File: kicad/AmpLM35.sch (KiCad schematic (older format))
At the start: 15 parts, among them P2 CONN_01X03, U1 OP07, U2 OP07

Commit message: circuito y pcb terminado.
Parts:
- removed P2: CONN_01X03, Pin_Headers:Pin_Header_Straight_1x03, symbol CONN_01X03
- added U6: LM35, TO_SOT_Packages_THT:TO-92_Inline_Wide, symbol LM35
- added W1: Lm1, Measurement_Points:Measurement_Point_Round-SMD-Pad_Big, symbol TEST_1P
- added W2: Lm2, Measurement_Points:Measurement_Point_Round-SMD-Pad_Big, symbol TEST_1P
- added W3: Lm3, Measurement_Points:Measurement_Point_Round-SMD-Pad_Big, symbol TEST_1P
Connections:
- net +5V: now also U6.1 (+Vs)
- net GNDA: now also U6.3 (GND)
- net LM35_OUT: now also W3.1
- net at U1.3 (+): now also U6.2 (Vout), W1.1
- net at R2.1, R3.2, U1.6: now also W2.1
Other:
- note added: "Capacitores de desacople\nDeben estar junto a U1"
- note added: "Capacitores de desacople\nDeben estar junto a U2"
- note added: "LM35 junto a la \nbornera de la \ntermocupla"
- note removed: "Capacitores de desacople\nEn el PCB deben estar junto a U1"
- note removed: "Capacitores de desacople\nEn el PCB deben estar junto a U2"
- note removed: "Conexión del LM35"
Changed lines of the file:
@@
 $Descr A4 11693 8268
 encoding utf-8
-Sheet 3 5
+Sheet 2 5
 Title "Amplificador y filtro del sensor LM35"
-Date "2016-08-27"
-Rev "1"
+Date "2016-09-11"
+Rev "2"
 Comp "Elián Hanisch - Rodrigo Oliver - Gastón Riera"
 Comment1 "Cátedra de Proyecto Final"
@@
 	1    0    0    -1
 $EndComp
-Text HLabel 2750 1850 0    60   Input ~ 0
-+5V
-Text HLabel 2750 2000 0    60   Input ~ 0
--5V
-Text HLabel 2750 2150 0    60   Input ~ 0
-GND
-$Comp
-L -5V #PWR6
-U 1 1 57C21C1D
-P 3350 1600
-F 0 "#PWR6" H 3350 1700 50  0001 C CNN
-F 1 "-5V" H 3350 1750 50  0000 C CNN
-F 2 "" H 3350 1600 50  0000 C CNN
-F 3 "" H 3350 1600 50  0000 C CNN
-	1    3350 1600
-	1    0    0    -1
-$EndComp
-$Comp
-L +5V #PWR03
-U 1 1 57C21BA8
-P 3100 1600
-F 0 "#PWR03" H 3100 1450 50  0001 C CNN
-F 1 "+5V" H 3100 1740 50  0000 C CNN
-F 2 "" H 3100 1600 50  0000 C CNN
-F 3 "" H 3100 1600 50  0000 C CNN
-	1    3100 1600
-	1    0    0    -1
-$EndComp
-$Comp
-L +5V #PWR04
+$Comp
+L +5V #PWR07
 U 1 1 57C21C9E
-P 1800 3100
-F 0 "#PWR04" H 1800 2950 50  0001 C CNN
-F 1 "+5V" H 1800 3240 50  0000 C CNN
-F 2 "" H 1800 3100 50  0000 C CNN
-F 3 "" H 1800 3100 50  0000 C CNN
-	1    1800 3100
-	1    0    0    -1
-$EndComp
-$Comp
-L -5V #PWR20
+P 2500 2950
+F 0 "#PWR07" H 2500 2800 50  0001 C CNN
+F 1 "+5V" H 2500 3090 50  0000 C CNN
+F 2 "" H 2500 2950 50  0000 C CNN
+F 3 "" H 2500 2950 50  0000 C CNN
+	1    2500 2950
+	1    0    0    -1
+$EndComp
+$Comp
+L -5V #PWR22
 U 1 1 57C21D19
 P 7850 3850
-F 0 "#PWR20" H 7850 3950 50  0001 C CNN
+F 0 "#PWR22" H 7850 3950 50  0001 C CNN
 F 1 "-5V" H 7850 4000 50  0000 C CNN
 F 2 "" H 7850 3850 50  0000 C CNN
@@
 $EndComp
 $Comp
-L -5V #PWR10
+L -5V #PWR12
 U 1 1 57C21D33
 P 4750 3800
-F 0 "#PWR10" H 4750 3900 50  0001 C CNN
+F 0 "#PWR12" H 4750 3900 50  0001 C CNN
 F 1 "-5V" H 4750 3950 50  0000 C CNN
 F 2 "" H 4750 3800 50  0000 C CNN
@@
 $EndComp
 $Comp
-L +5V #PWR05
+L +5V #PWR08
 U 1 1 57C21D4D
 P 4750 3150
-F 0 "#PWR05" H 4750 3000 50  0001 C CNN
+F 0 "#PWR08" H 4750 3000 50  0001 C CNN
 F 1 "+5V" H 4750 3290 50  0000 C CNN
 F 2 "" H 4750 3150 50  0000 C CNN
@@
 $EndComp
 $Comp
-L +5V #PWR06
+L +5V #PWR09
 U 1 1 57C21D67
 P 7850 3250
-F 0 "#PWR06" H 7850 3100 50  0001 C CNN
+F 0 "#PWR09" H 7850 3100 50  0001 C CNN
 F 1 "+5V" H 7850 3390 50  0000 C CNN
 F 2 "" H 7850 3250 50  0000 C CNN
@@
 LM35_OUT
 $Comp
-L GNDA #PWR07
+L GNDA #PWR010
 U 1 1 57C21F0E
-P 1800 3600
-F 0 "#PWR07" H 1800 3350 50  0001 C CNN
-F 1 "GNDA" H 1800 3450 50  0000 C CNN
-F 2 "" H 1800 3600 50  0000 C CNN
-F 3 "" H 1800 3600 50  0000 C CNN
-	1    1800 3600
-	1    0    0    -1
-$EndComp
-$Comp
-L GNDA #PWR08
-U 1 1 57C21F2C
-P 3350 2250
-F 0 "#PWR08" H 3350 2000 50  0001 C CNN
-F 1 "GNDA" H 3350 2100 50  0000 C CNN
-F 2 "" H 3350 2250 50  0000 C CNN
-F 3 "" H 3350 2250 50  0000 C CNN
-	1    3350 2250
+P 2500 3750
+F 0 "#PWR010" H 2500 3500 50  0001 C CNN
+F 1 "GNDA" H 2500 3600 50  0000 C CNN
+F 2 "" H 2500 3750 50  0000 C CNN
+F 3 "" H 2500 3750 50  0000 C CNN
+	1    2500 3750
 	1    0    0    -1
 $EndComp
@@
 $EndComp
 $Comp
-L GNDA #PWR09
+L GNDA #PWR011
 U 1 1 57C224B9
 P 7300 4550
-F 0 "#PWR09" H 7300 4300 50  0001 C CNN
+F 0 "#PWR011" H 7300 4300 50  0001 C CNN
 F 1 "GNDA" H 7300 4400 50  0000 C CNN
 F 2 "" H 7300 4550 50  0000 C CNN
@@
 $EndComp
 $Comp
-L GNDA #PWR010
+L GNDA #PWR012
 U 1 1 57C228B2
 P 3900 4800
-F 0 "#PWR010" H 3900 4550 50  0001 C CNN
+F 0 "#PWR012" H 3900 4550 50  0001 C CNN
 F 1 "GNDA" H 3900 4650 50  0000 C CNN
 F 2 "" H 3900 4800 50  0000 C CNN
@@
 P 8200 4750
 F 0 "RV2" H 8200 4670 50  0000 C CNN
-F 1 "POT" H 8200 4750 50  0000 C CNN
+F 1 "POT" H 8200 4750 50  0001 C CNN
 F 2 "Potentiometers:Potentiometer_Bourns_3005_Angular_ScrewFront" H 8200 4750 50  0001 C CNN
 F 3 "" H 8200 4750 50  0000 C CNN
@@
 $EndComp
 $Comp
-L +5V #PWR011
+L +5V #PWR013
 U 1 1 57C51F8E
 P 8350 4450
-F 0 "#PWR011" H 8350 4300 50  0001 C CNN
+F 0 "#PWR013" H 8350 4300 50  0001 C CNN
 F 1 "+5V" H 8350 4590 50  0000 C CNN
 F 2 "" H 8350 4450 50  0000 C CNN
@@
 P 5100 4750
 F 0 "RV1" H 5100 4670 50  0000 C CNN
-F 1 "POT" H 5100 4750 50  0000 C CNN
+F 1 "POT" H 5100 4750 50  0001 C CNN
 F 2 "Potentiometers:Potentiometer_Bourns_3005_Angular_ScrewFront" H 5100 4750 50  0001 C CNN
 F 3 "" H 5100 4750 50  0000 C CNN
@@
 $EndComp
 $Comp
-L +5V #PWR012
+L +5V #PWR014
 U 1 1 57C5230B
 P 5250 4450
-F 0 "#PWR012" H 5250 4300 50  0001 C CNN
+F 0 "#PWR014" H 5250 4300 50  0001 C CNN
 F 1 "+5V" H 5250 4590 50  0000 C CNN
 F 2 "" H 5250 4450 50  0000 C CNN
@@
 	1    0    0    -1
 $EndComp
-$Comp
-L CONN_01X03 P2
-U 1 1 57C53794
-P 1550 3350
-F 0 "P2" H 1550 3550 50  0000 C CNN
-F 1 "CONN_01X03" V 1650 3350 50  0000 C CNN
-F 2 "Pin_Headers:Pin_Header_Straight_1x03" H 1550 3350 50  0001 C CNN
-F 3 "" H 1550 3350 50  0000 C CNN
-	1    1550 3350
-	-1   0    0    1
-$EndComp
-Text Notes 1500 2850 0    60   ~ 0
-Conexión del LM35
+Text Notes 2250 4250 0    60   ~ 0
+LM35 junto a la \nbornera de la \ntermocupla
 Text Notes 7500 2600 0    60   ~ 0
 Filtro pasa-bajos\nFc = 2Hz\nAtt@50hz = 40dB
@@
 $EndComp
 $Comp
-L GNDA #PWR013
+L GNDA #PWR015
 U 1 1 57C5CD5D
 P 7800 5750
-F 0 "#PWR013" H 7800 5500 50  0001 C CNN
+F 0 "#PWR015" H 7800 5500 50  0001 C CNN
 F 1 "GNDA" H 7800 5600 50  0000 C CNN
 F 2 "" H 7800 5750 50  0000 C CNN
@@
 $EndComp
 $Comp
-L GNDA #PWR014
+L GNDA #PWR016
 U 1 1 57C5CD63
 P 8200 5750
-F 0 "#PWR014" H 8200 5500 50  0001 C CNN
+F 0 "#PWR016" H 8200 5500 50  0001 C CNN
 F 1 "GNDA" H 8200 5600 50  0000 C CNN
 F 2 "" H 8200 5750 50  0000 C CNN
@@
 $EndComp
 $Comp
-L +5V #PWR015
+L +5V #PWR017
 U 1 1 57C5CD69
 P 7800 5450
-F 0 "#PWR015" H 7800 5300 50  0001 C CNN
+F 0 "#PWR017" H 7800 5300 50  0001 C CNN
 F 1 "+5V" H 7800 5590 50  0000 C CNN
 F 2 "" H 7800 5450 50  0000 C CNN
@@
 $EndComp
 $Comp
-L -5V #PWR21
+L -5V #PWR23
 U 1 1 57C5CD6F
 P 8200 5450
-F 0 "#PWR21" H 8200 5550 50  0001 C CNN
+F 0 "#PWR23" H 8200 5550 50  0001 C CNN
 F 1 "-5V" H 8200 5600 50  0000 C CNN
 F 2 "" H 8200 5450 50  0000 C CNN
@@
 $EndComp
 Text Notes 7750 6150 0    60   ~ 0
-Capacitores de desacople\nEn el PCB deben estar junto a U2
+Capacitores de desacople\nDeben estar junto a U2
 $Comp
 L C C5
@@
 $EndComp
 $Comp
-L GNDA #PWR016
+L GNDA #PWR018
 U 1 1 57C5D25F
 P 4900 5750
-F 0 "#PWR016" H 4900 5500 50  0001 C CNN
+F 0 "#PWR018" H 4900 5500 50  0001 C CNN
 F 1 "GNDA" H 4900 5600 50  0000 C CNN
 F 2 "" H 4900 5750 50  0000 C CNN
@@
 $EndComp
 $Comp
-L GNDA #PWR017
+L GNDA #PWR019
 U 1 1 57C5D265
 P 5300 5750
-F 0 "#PWR017" H 5300 5500 50  0001 C CNN
+F 0 "#PWR019" H 5300 5500 50  0001 C CNN
 F 1 "GNDA" H 5300 5600 50  0000 C CNN
 F 2 "" H 5300 5750 50  0000 C CNN
@@
 $EndComp
 $Comp
-L +5V #PWR018
+L +5V #PWR020
 U 1 1 57C5D26B
 P 4900 5450
-F 0 "#PWR018" H 4900 5300 50  0001 C CNN
+F 0 "#PWR020" H 4900 5300 50  0001 C CNN
 F 1 "+5V" H 4900 5590 50  0000 C CNN
 F 2 "" H 4900 5450 50  0000 C CNN
@@
 $EndComp
 $Comp
-L -5V #PWR14
+L -5V #PWR16
 U 1 1 57C5D271
 P 5300 5450
-F 0 "#PWR14" H 5300 5550 50  0001 C CNN
+F 0 "#PWR16" H 5300 5550 50  0001 C CNN
 F 1 "-5V" H 5300 5600 50  0000 C CNN
 F 2 "" H 5300 5450 50  0000 C CNN
@@
 $EndComp
 Text Notes 4850 6150 0    60   ~ 0
-Capacitores de desacople\nEn el PCB deben estar junto a U1
-Wire Wire Line
-	3100 1600 3100 1850
-Wire Wire Line
-	3100 1850 2750 1850
+Capacitores de desacople\nDeben estar junto a U1
 Wire Wire Line
 	9350 3550 8250 3550
@@
 	7300 4150 7300 4550
 Wire Wire Line
-	1750 3350 4550 3350
-Wire Wire Line
 	3900 3550 4550 3550
 Wire Wire Line
@@
 	5250 4450 5250 4750
 Wire Wire Line
-	1800 3100 1800 3250
-Wire Wire Line
-	1800 3250 1750 3250
-Wire Wire Line
-	1750 3450 1800 3450
-Wire Wire Line
-	1800 3450 1800 3600
-Wire Wire Line
-	2750 2000 3350 2000
-Wire Wire Line
-	3350 2000 3350 1600
-Wire Wire Line
-	2750 2150 3350 2150
-Wire Wire Line
-	3350 2150 3350 2250
-Wire Wire Line
 	4750 3750 4750 3800
+$Comp
+L LM35 U6
+U 1 1 57D19F7B
+P 2500 3350
+F 0 "U6" H 2150 3400 50  0000 C CNN
+F 1 "LM35" H 2150 3300 50  0000 C CNN
+F 2 "TO_SOT_Packages_THT:TO-92_Inline_Wide" H 2500 3600 50  0001 C CNN
+F 3 "" H 2500 3600 50  0000 C CNN
+	1    2500 3350
+	1    0    0    -1
+$EndComp
+Wire Wire Line
+	4550 3350 2800 3350
+$Comp
+L TEST_1P W1
+U 1 1 57D4AAF4
+P 3650 3200
+F 0 "W1" H 3650 3470 50  0000 C CNN
+F 1 "Lm1" H 3650 3400 50  0000 C CNN
+F 2 "Measurement_Points:Measurement_Point_Round-SMD-Pad_Big" H 3850 3200 50  0001 C CNN
+F 3 "" H 3850 3200 50  0000 C CNN
+	1    3650 3200
+	1    0    0    -1
+$EndComp
+Wire Wire Line
+	3650 3200 3650 3350
+Connection ~ 3650 3350
+$Comp
+L TEST_1P W2
+U 1 1 57D4B518
+P 5700 3250
+F 0 "W2" H 5700 3520 50  0000 C CNN
+F 1 "Lm2" H 5700 3450 50  0000 C CNN
+F 2 "Measurement_Points:Measurement_Point_Round-SMD-Pad_Big" H 5900 3250 50  0001 C CNN
+F 3 "" H 5900 3250 50  0000 C CNN
+	1    5700 3250
+	1    0    0    -1
+$EndComp
+Wire Wire Line
+	5700 3250 5700 3450
+Connection ~ 5700 3450
+$Comp
+L TEST_1P W3
+U 1 1 57D4BC1D
+P 9150 3300
+F 0 "W3" H 9150 3570 50  0000 C CNN
+F 1 "Lm3" H 9150 3500 50  0000 C CNN
+F 2 "Measurement_Points:Measurement_Point_Round-SMD-Pad_Big" H 9350 3300 50  0001 C CNN
+F 3 "" H 9350 3300 50  0000 C CNN
+	1    9150 3300
+	1    0    0    -1
+$EndComp
+Wire Wire Line
+	9150 3300 9150 3550
+Connection ~ 9150 3550
 $EndSCHEMATC

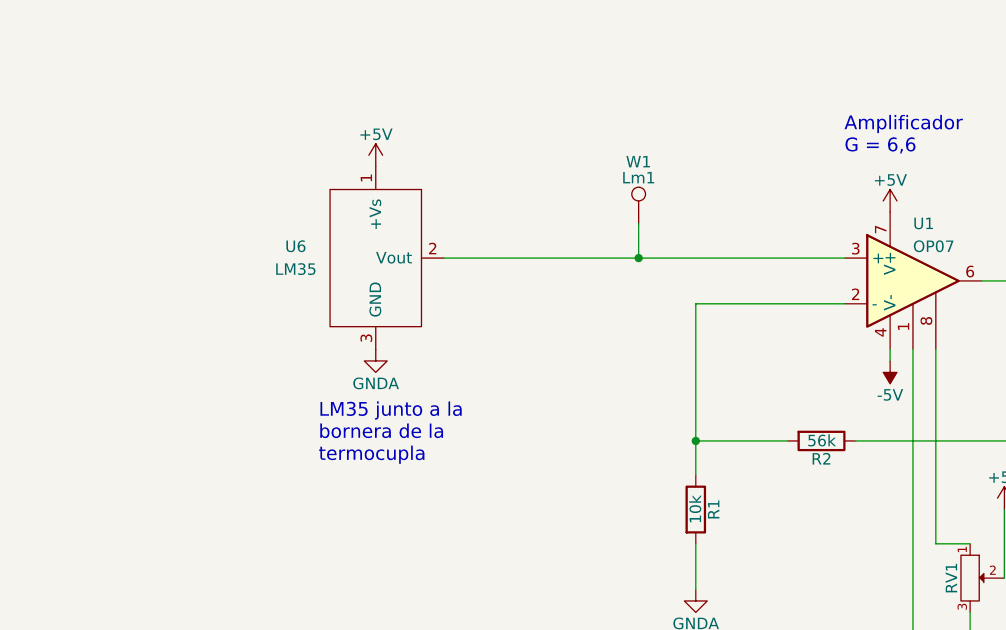
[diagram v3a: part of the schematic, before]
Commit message: actualizar el esquematico rev3
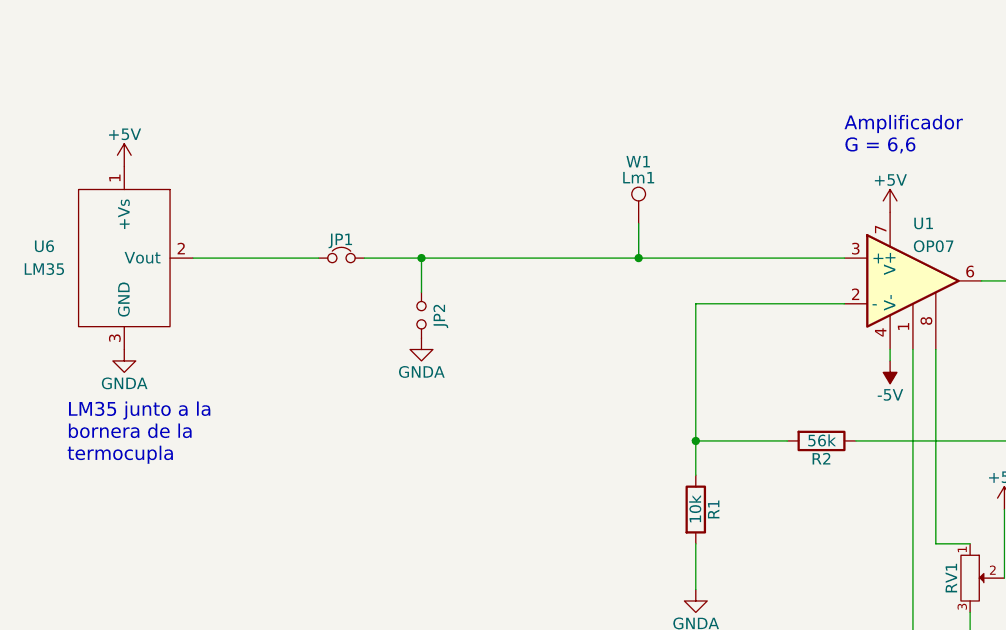
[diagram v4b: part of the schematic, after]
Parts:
- added JP1: Jumper_NC_Small, symbol Jumper_NC_Small
- added JP2: Jumper_NO_Small, symbol Jumper_NO_Small
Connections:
- net GNDA: now also JP2.2
- net at U1.3 (+), W1.1: now also JP1.2, JP2.1; no longer U6.2 (Vout)
- new net: JP1.1, U6.2 (Vout)
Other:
- moved on the sheet: U6
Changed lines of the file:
@@
 Sheet 2 5
 Title "Amplificador y filtro del sensor LM35"
-Date "2016-09-11"
-Rev "2"
+Date "2016-11-10"
+Rev "3"
 Comp "Elián Hanisch - Rodrigo Oliver - Gastón Riera"
 Comment1 "Cátedra de Proyecto Final"
@@
 L +5V #PWR10
 U 1 1 57C21C9E
-P 2500 2950
-F 0 "#PWR10" H 2500 2800 50  0001 C CNN
-F 1 "+5V" H 2500 3090 50  0000 C CNN
-F 2 "" H 2500 2950 50  0000 C CNN
-F 3 "" H 2500 2950 50  0000 C CNN
-	1    2500 2950
-	1    0    0    -1
-$EndComp
-$Comp
-L -5V #PWR24
+P 1400 2950
+F 0 "#PWR10" H 1400 2800 50  0001 C CNN
+F 1 "+5V" H 1400 3090 50  0000 C CNN
+F 2 "" H 1400 2950 50  0000 C CNN
+F 3 "" H 1400 2950 50  0000 C CNN
+	1    1400 2950
+	1    0    0    -1
+$EndComp
+$Comp
+L -5V #PWR25
 U 1 1 57C21D19
 P 7850 3850
-F 0 "#PWR24" H 7850 3950 50  0001 C CNN
+F 0 "#PWR25" H 7850 3950 50  0001 C CNN
 F 1 "-5V" H 7850 4000 50  0000 C CNN
 F 2 "" H 7850 3850 50  0000 C CNN
@@
 $EndComp
 $Comp
-L -5V #PWR14
+L -5V #PWR15
 U 1 1 57C21D33
 P 4750 3800
-F 0 "#PWR14" H 4750 3900 50  0001 C CNN
+F 0 "#PWR15" H 4750 3900 50  0001 C CNN
 F 1 "-5V" H 4750 3950 50  0000 C CNN
 F 2 "" H 4750 3800 50  0000 C CNN
@@
 $EndComp
 $Comp
-L +5V #PWR13
+L +5V #PWR14
 U 1 1 57C21D4D
 P 4750 3150
-F 0 "#PWR13" H 4750 3000 50  0001 C CNN
+F 0 "#PWR14" H 4750 3000 50  0001 C CNN
 F 1 "+5V" H 4750 3290 50  0000 C CNN
 F 2 "" H 4750 3150 50  0000 C CNN
@@
 $EndComp
 $Comp
-L +5V #PWR23
+L +5V #PWR24
 U 1 1 57C21D67
 P 7850 3250
-F 0 "#PWR23" H 7850 3100 50  0001 C CNN
+F 0 "#PWR24" H 7850 3100 50  0001 C CNN
 F 1 "+5V" H 7850 3390 50  0000 C CNN
 F 2 "" H 7850 3250 50  0000 C CNN
@@
 L GNDA #PWR11
 U 1 1 57C21F0E
-P 2500 3750
-F 0 "#PWR11" H 2500 3500 50  0001 C CNN
-F 1 "GNDA" H 2500 3600 50  0000 C CNN
-F 2 "" H 2500 3750 50  0000 C CNN
-F 3 "" H 2500 3750 50  0000 C CNN
-	1    2500 3750
+P 1400 3750
+F 0 "#PWR11" H 1400 3500 50  0001 C CNN
+F 1 "GNDA" H 1400 3600 50  0000 C CNN
+F 2 "" H 1400 3750 50  0000 C CNN
+F 3 "" H 1400 3750 50  0000 C CNN
+	1    1400 3750
 	1    0    0    -1
 $EndComp
@@
 $EndComp
 $Comp
-L GNDA #PWR20
+L GNDA #PWR21
 U 1 1 57C224B9
 P 7300 4550
-F 0 "#PWR20" H 7300 4300 50  0001 C CNN
+F 0 "#PWR21" H 7300 4300 50  0001 C CNN
 F 1 "GNDA" H 7300 4400 50  0000 C CNN
 F 2 "" H 7300 4550 50  0000 C CNN
@@
 $EndComp
 $Comp
-L GNDA #PWR12
+L GNDA #PWR13
 U 1 1 57C228B2
 P 3900 4800
-F 0 "#PWR12" H 3900 4550 50  0001 C CNN
+F 0 "#PWR13" H 3900 4550 50  0001 C CNN
 F 1 "GNDA" H 3900 4650 50  0000 C CNN
 F 2 "" H 3900 4800 50  0000 C CNN
@@
 $EndComp
 $Comp
-L +5V #PWR27
+L +5V #PWR28
 U 1 1 57C51F8E
 P 8350 4450
-F 0 "#PWR27" H 8350 4300 50  0001 C CNN
+F 0 "#PWR28" H 8350 4300 50  0001 C CNN
 F 1 "+5V" H 8350 4590 50  0000 C CNN
 F 2 "" H 8350 4450 50  0000 C CNN
@@
 $EndComp
 $Comp
-L +5V #PWR17
+L +5V #PWR18
 U 1 1 57C5230B
 P 5250 4450
-F 0 "#PWR17" H 5250 4300 50  0001 C CNN
+F 0 "#PWR18" H 5250 4300 50  0001 C CNN
 F 1 "+5V" H 5250 4590 50  0000 C CNN
 F 2 "" H 5250 4450 50  0000 C CNN
@@
 	1    0    0    -1
 $EndComp
-Text Notes 2250 4250 0    60   ~ 0
+Text Notes 1150 4250 0    60   ~ 0
 LM35 junto a la \nbornera de la \ntermocupla
 Text Notes 7500 2600 0    60   ~ 0
@@
 $EndComp
 $Comp
-L GNDA #PWR22
+L GNDA #PWR23
 U 1 1 57C5CD5D
 P 7800 5750
-F 0 "#PWR22" H 7800 5500 50  0001 C CNN
+F 0 "#PWR23" H 7800 5500 50  0001 C CNN
 F 1 "GNDA" H 7800 5600 50  0000 C CNN
 F 2 "" H 7800 5750 50  0000 C CNN
@@
 $EndComp
 $Comp
-L GNDA #PWR26
+L GNDA #PWR27
 U 1 1 57C5CD63
 P 8200 5750
-F 0 "#PWR26" H 8200 5500 50  0001 C CNN
+F 0 "#PWR27" H 8200 5500 50  0001 C CNN
 F 1 "GNDA" H 8200 5600 50  0000 C CNN
 F 2 "" H 8200 5750 50  0000 C CNN
@@
 $EndComp
 $Comp
-L +5V #PWR21
+L +5V #PWR22
 U 1 1 57C5CD69
 P 7800 5450
-F 0 "#PWR21" H 7800 5300 50  0001 C CNN
+F 0 "#PWR22" H 7800 5300 50  0001 C CNN
 F 1 "+5V" H 7800 5590 50  0000 C CNN
 F 2 "" H 7800 5450 50  0000 C CNN
@@
 $EndComp
 $Comp
-L -5V #PWR25
+L -5V #PWR26
 U 1 1 57C5CD6F
 P 8200 5450
-F 0 "#PWR25" H 8200 5550 50  0001 C CNN
+F 0 "#PWR26" H 8200 5550 50  0001 C CNN
 F 1 "-5V" H 8200 5600 50  0000 C CNN
 F 2 "" H 8200 5450 50  0000 C CNN
@@
 $EndComp
 $Comp
-L GNDA #PWR16
+L GNDA #PWR17
 U 1 1 57C5D25F
 P 4900 5750
-F 0 "#PWR16" H 4900 5500 50  0001 C CNN
+F 0 "#PWR17" H 4900 5500 50  0001 C CNN
 F 1 "GNDA" H 4900 5600 50  0000 C CNN
 F 2 "" H 4900 5750 50  0000 C CNN
@@
 $EndComp
 $Comp
-L GNDA #PWR19
+L GNDA #PWR20
 U 1 1 57C5D265
 P 5300 5750
-F 0 "#PWR19" H 5300 5500 50  0001 C CNN
+F 0 "#PWR20" H 5300 5500 50  0001 C CNN
 F 1 "GNDA" H 5300 5600 50  0000 C CNN
 F 2 "" H 5300 5750 50  0000 C CNN
@@
 $EndComp
 $Comp
-L +5V #PWR15
+L +5V #PWR16
 U 1 1 57C5D26B
 P 4900 5450
-F 0 "#PWR15" H 4900 5300 50  0001 C CNN
+F 0 "#PWR16" H 4900 5300 50  0001 C CNN
 F 1 "+5V" H 4900 5590 50  0000 C CNN
 F 2 "" H 4900 5450 50  0000 C CNN
@@
 $EndComp
 $Comp
-L -5V #PWR18
+L -5V #PWR19
 U 1 1 57C5D271
 P 5300 5450
-F 0 "#PWR18" H 5300 5550 50  0001 C CNN
+F 0 "#PWR19" H 5300 5550 50  0001 C CNN
 F 1 "-5V" H 5300 5600 50  0000 C CNN
 F 2 "" H 5300 5450 50  0000 C CNN
@@
 L LM35 U6
 U 1 1 57D19F7B
-P 2500 3350
-F 0 "U6" H 2150 3400 50  0000 C CNN
-F 1 "LM35" H 2150 3300 50  0000 C CNN
-F 2 "TO_SOT_Packages_THT:TO-92_Inline_Wide" H 2500 3600 50  0001 C CNN
-F 3 "" H 2500 3600 50  0000 C CNN
-	1    2500 3350
-	1    0    0    -1
-$EndComp
-Wire Wire Line
-	4550 3350 2800 3350
+P 1400 3350
+F 0 "U6" H 1050 3400 50  0000 C CNN
+F 1 "LM35" H 1050 3300 50  0000 C CNN
+F 2 "TO_SOT_Packages_THT:TO-92_Inline_Wide" H 1400 3600 50  0001 C CNN
+F 3 "" H 1400 3600 50  0000 C CNN
+	1    1400 3350
+	1    0    0    -1
+$EndComp
 $Comp
 L TEST_1P W1
@@
 	9150 3300 9150 3550
 Connection ~ 9150 3550
+$Comp
+L Jumper_NC_Small JP1
+U 1 1 582F4F7A
+P 2350 3350
+F 0 "JP1" H 2350 3430 50  0000 C CNN
+F 1 "Jumper_NC_Small" H 2360 3290 50  0001 C CNN
+F 2 "" H 2350 3350 50  0000 C CNN
+F 3 "" H 2350 3350 50  0000 C CNN
+	1    2350 3350
+	1    0    0    -1
+$EndComp
+$Comp
+L Jumper_NO_Small JP2
+U 1 1 582F4FC5
+P 2700 3600
+F 0 "JP2" H 2700 3680 50  0000 C CNN
+F 1 "Jumper_NO_Small" H 2710 3540 50  0001 C CNN
+F 2 "" H 2700 3600 50  0000 C CNN
+F 3 "" H 2700 3600 50  0000 C CNN
+	1    2700 3600
+	0    1    1    0
+$EndComp
+Wire Wire Line
+	1700 3350 2250 3350
+Wire Wire Line
+	2450 3350 4550 3350
+Wire Wire Line
+	2700 3500 2700 3350
+Connection ~ 2700 3350
+$Comp
+L GNDA #PWR12
+U 1 1 582F516B
+P 2700 3700
+F 0 "#PWR12" H 2700 3450 50  0001 C CNN
+F 1 "GNDA" H 2700 3550 50  0000 C CNN
+F 2 "" H 2700 3700 50  0000 C CNN
+F 3 "" H 2700 3700 50  0000 C CNN
+	1    2700 3700
+	1    0    0    -1
+$EndComp
 $EndSCHEMATC
